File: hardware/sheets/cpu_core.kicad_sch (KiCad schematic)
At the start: 25 parts, among them U1 V20, U10 74HC32, U11 74HC08, U12 74HC157, U13 74HC04, U14 TCM809, U15 74HC08, U2 74HC573, U3 74HC573, U4 74HC573, U5 74HC245, U6 74HCT138, U7 74HC00, U8 74HC74, U9 74HC4017

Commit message: Standardize 5V glue on 74HCT; fix bus-latch family; div-3 -> 74HCT163
All 5V 74-series logic moved from mixed HC/HCT to 74HCT (TTL thresholds reliably
read 3.3V level-shifter outputs). Fixes the address latches / data transceiver
that were wrongly 74HC instead of the design's 74HCT. The div-by-3 moves from
74HC4017 (no HCT variant) to a 74HCT163 preset-to-3 with a spare 74HCT04 gate
for the TC->~PE reload. Per-card level shifters use a dedicated 74LVC245A symbol.
Pinouts unchanged; netlist intact; zero structural ERC errors.

Co-Authored-By: Claude Opus 4.8 (1M context) <noreply@anthropic.com>
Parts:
- removed U10: 74HC32, symbol mini-xt:74HC32
- removed U11, U15: 74HC08, symbol mini-xt:74HC08
- removed U12: 74HC157, symbol mini-xt:74HC157
- removed U13: 74HC04, symbol mini-xt:74HC04
- removed U2, U3, U4: 74HC573, symbol mini-xt:74HC573
- removed U5: 74HC245, symbol mini-xt:74HC245
- removed U7: 74HC00, symbol mini-xt:74HC00
- removed U8: 74HC74, symbol mini-xt:74HC74
- removed U9: 74HC4017, symbol mini-xt:74HC4017
- added U10: 74HCT32, symbol mini-xt:74HCT32
- added U11, U15: 74HCT08, symbol mini-xt:74HCT08
- added U12: 74HCT157, symbol mini-xt:74HCT157
- added U13: 74HCT04, symbol mini-xt:74HCT04
- added U2, U3, U4: 74HCT573, symbol mini-xt:74HCT573
- added U5: 74HCT245, symbol mini-xt:74HCT245
- added U7: 74HCT00, symbol mini-xt:74HCT00
- added U8: 74HCT74, symbol mini-xt:74HCT74
- added U9: 74HCT163, symbol mini-xt:74HCT163
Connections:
- net +5V: now also U10.14 (VCC), U11.14 (VCC), U12.16 (VCC), U13.14 (VCC), U15.14 (VCC), U2.20 (VCC), U3.20 (VCC), U4.20 (VCC), U5.20 (VCC), U7.14 (VCC), U8.1 (~{R}), U8.14 (VCC), U8.4 (~{S}), U9.1 (~{MR}), U9.10 (CET), U9.16 (VCC), U9.3 (D0), U9.5 (D2), U9.6 (D3), U9.7 (CEP)
- net A0: now also U2.19 (Q0)
- net A1: now also U2.18 (Q1)
- net A10: now also U3.17 (Q2)
- net A11: now also U3.16 (Q3)
- net A12: now also U3.15 (Q4)
- net A13: now also U3.14 (Q5)
- net A14: now also U3.13 (Q6)
- net A15: now also U3.12 (Q7)
- net A16: now also U4.19 (Q0)
- net A17: now also U4.18 (Q1)
- net A18: now also U4.17 (Q2)
- net A19: now also U4.16 (Q3), U7.1 (P1)
- net A2: now also U2.17 (Q2)
- net A3: now also U2.16 (Q3)
- net A4: now also U2.15 (Q4)
- net A5: now also U2.14 (Q5)
- net A6: now also U2.13 (Q6)
- net A7: now also U2.12 (Q7)
- net A8: now also U3.19 (Q0)
- net A9: now also U3.18 (Q1)
- net AD0: now also U2.2 (D0), U5.2 (A0)
- net AD1: now also U2.3 (D1), U5.3 (A1)
- net AD2: now also U2.4 (D2), U5.4 (A2)
- net AD3: now also U2.5 (D3), U5.5 (A3)
- net AD4: now also U2.6 (D4), U5.6 (A4)
- net AD5: now also U2.7 (D5), U5.7 (A5)
- net AD6: now also U2.8 (D6), U5.8 (A6)
- net AD7: now also U2.9 (D7), U5.9 (A7)
- net BALE_L: now also U2.11 (Load), U3.11 (Load), U4.11 (Load)
- net CLK: now also U13.4 (P4)
- net CLK4: now also U12.3 (I1a), U9.14 (Q0)
- net CLK7: now also U12.2 (I0a), U13.3 (P3), U8.5 (Q)
- net CLK_MUX: now also U12.4 (Za), U13.1 (P1)
- net CLK_QN: now also U8.2 (D), U8.6 (~{Q})
- net CPUCLK: now also U13.2 (P2)
- net D0: now also U5.18 (B0)
- net D1: now also U5.17 (B1)
- net D2: now also U5.16 (B2)
- net D3: now also U5.15 (B3)
- net D4: now also U5.14 (B4)
- net D5: now also U5.13 (B5)
- net D6: now also U5.12 (B6)
- net D7: now also U5.11 (B7)
- net GND: now also U10.7 (GND), U11.7 (GND), U12.15 (E), U12.8 (GND), U13.7 (GND), U15.7 (GND), U2.1 (OE), U2.10 (GND), U3.1 (OE), U3.10 (GND), U4.1 (OE), U4.10 (GND), U5.10 (GND), U5.19 (CE), U7.7 (GND), U8.7 (GND), U9.4 (D1), U9.8 (GND)
- net MA10: now also U3.4 (D2)
- net MA11: now also U3.5 (D3)
- net MA12: now also U3.6 (D4)
- net MA13: now also U3.7 (D5)
- net MA14: now also U3.8 (D6)
- net MA15: now also U3.9 (D7)
- net MA16: now also U4.2 (D0)
- net MA17: now also U4.3 (D1)
- net MA18: now also U4.4 (D2)
- net MA19: now also U4.5 (D3)
- net MA8: now also U3.2 (D0)
- net MA9: now also U3.3 (D1)
- net OSC: now also U8.3 (C), U9.2 (CP)
- net RAM2_CE: now also U7.3 (P3)
- net SPEED_SEL: now also U12.1 (S)
- net Y5_INT: now also U7.2 (P2)
- net ~{IOR}: now also U10.13 (P13)
- net ~{IOW}: now also U11.13 (P13)
- net ~{MEMR}: now also U10.1 (P1)
- net ~{MEMW}: now also U11.1 (P1)
- net ~{RD}: now also U5.1 (A->B)
- new net DIV3_LD: U13.6 (P6), U9.9 (~{PE})
- new net DIV3_TC: U13.5 (P5), U9.15 (TC)

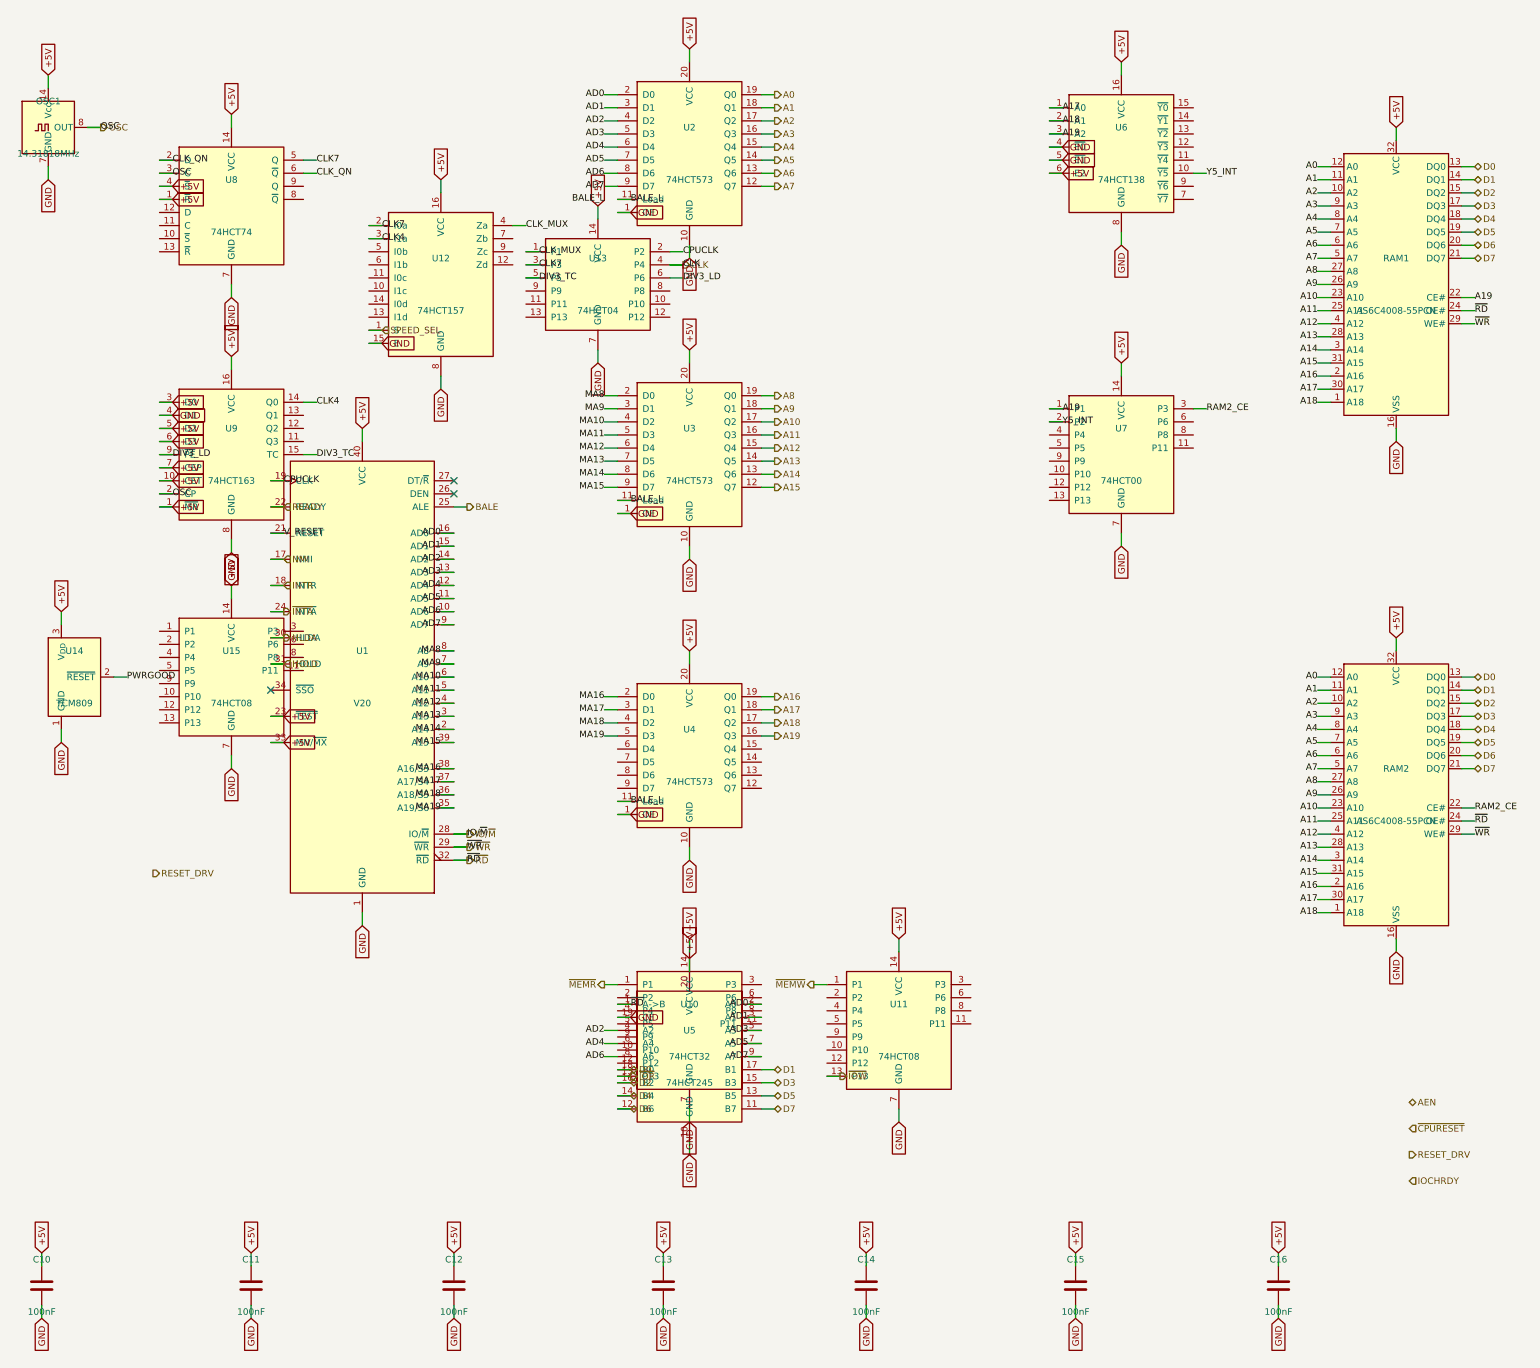
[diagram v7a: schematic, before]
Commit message: Fix all critical+high design-review findings (C1-C5, H1-H8)
Full review in hardware/notes/design-review-2026-07-03.md (with per-item
fix logs). Highlights:
- SRAM strobed by gated MEMR/MEMW (was raw ~RD/~WR: I/O cycles corrupted
  SRAM and the boot shadow-load could never write it)
- Reset chain implemented: NAND combine of ~PWRGOOD + ~CPURESET drives
  V20 RESET and an always-driven RESET_DRV (dropped from the Bus MCU)
- Contention-free bus handoff: '573 OE=HLDA vs counter '244 stage
  ~OE=~HLDA; strobe gates wired + tri-stated ('125, ~OE=HLDA); Bus MCU
  address group fixed to sense; AEN/TC fixed drive; BALE input-only
- '573 LE driven by BALE (was a dangling BALE_L label)
- Data '245 DIR=DT/~R, ~OE=DEN so INTA vectors reach the CPU
- Idle pulls: strobes/DEN high, AEN/IRQ2-9/DRQ low, IOCHRDY/IOCHCK/
  DACK2-3 high
- CH224K CFG1 left open (grounding it selects 9-20V, not 5V)
- XT-IDE INTRQ pull-down (pull-up parked IRQ5 asserted)
- LPT status bit7 = ~Busy via spare inverter (SPP semantics)
- Audio summer TL072 -> MCP6002 (RRIO; TL072 out of spec at +5V single
  supply)
- card_isatest: DUT P-FET gate to V5RAW + NPN driver (default off, can
  fully turn off); /3 divider TC->~PE reload actually wired

Overturned picks corrected in notes/questions-*.md. All sheets + cards
rebuilt; structural ERC = 0; fixes netlist-verified.

Co-Authored-By: Claude Fable 5 <noreply@anthropic.com>
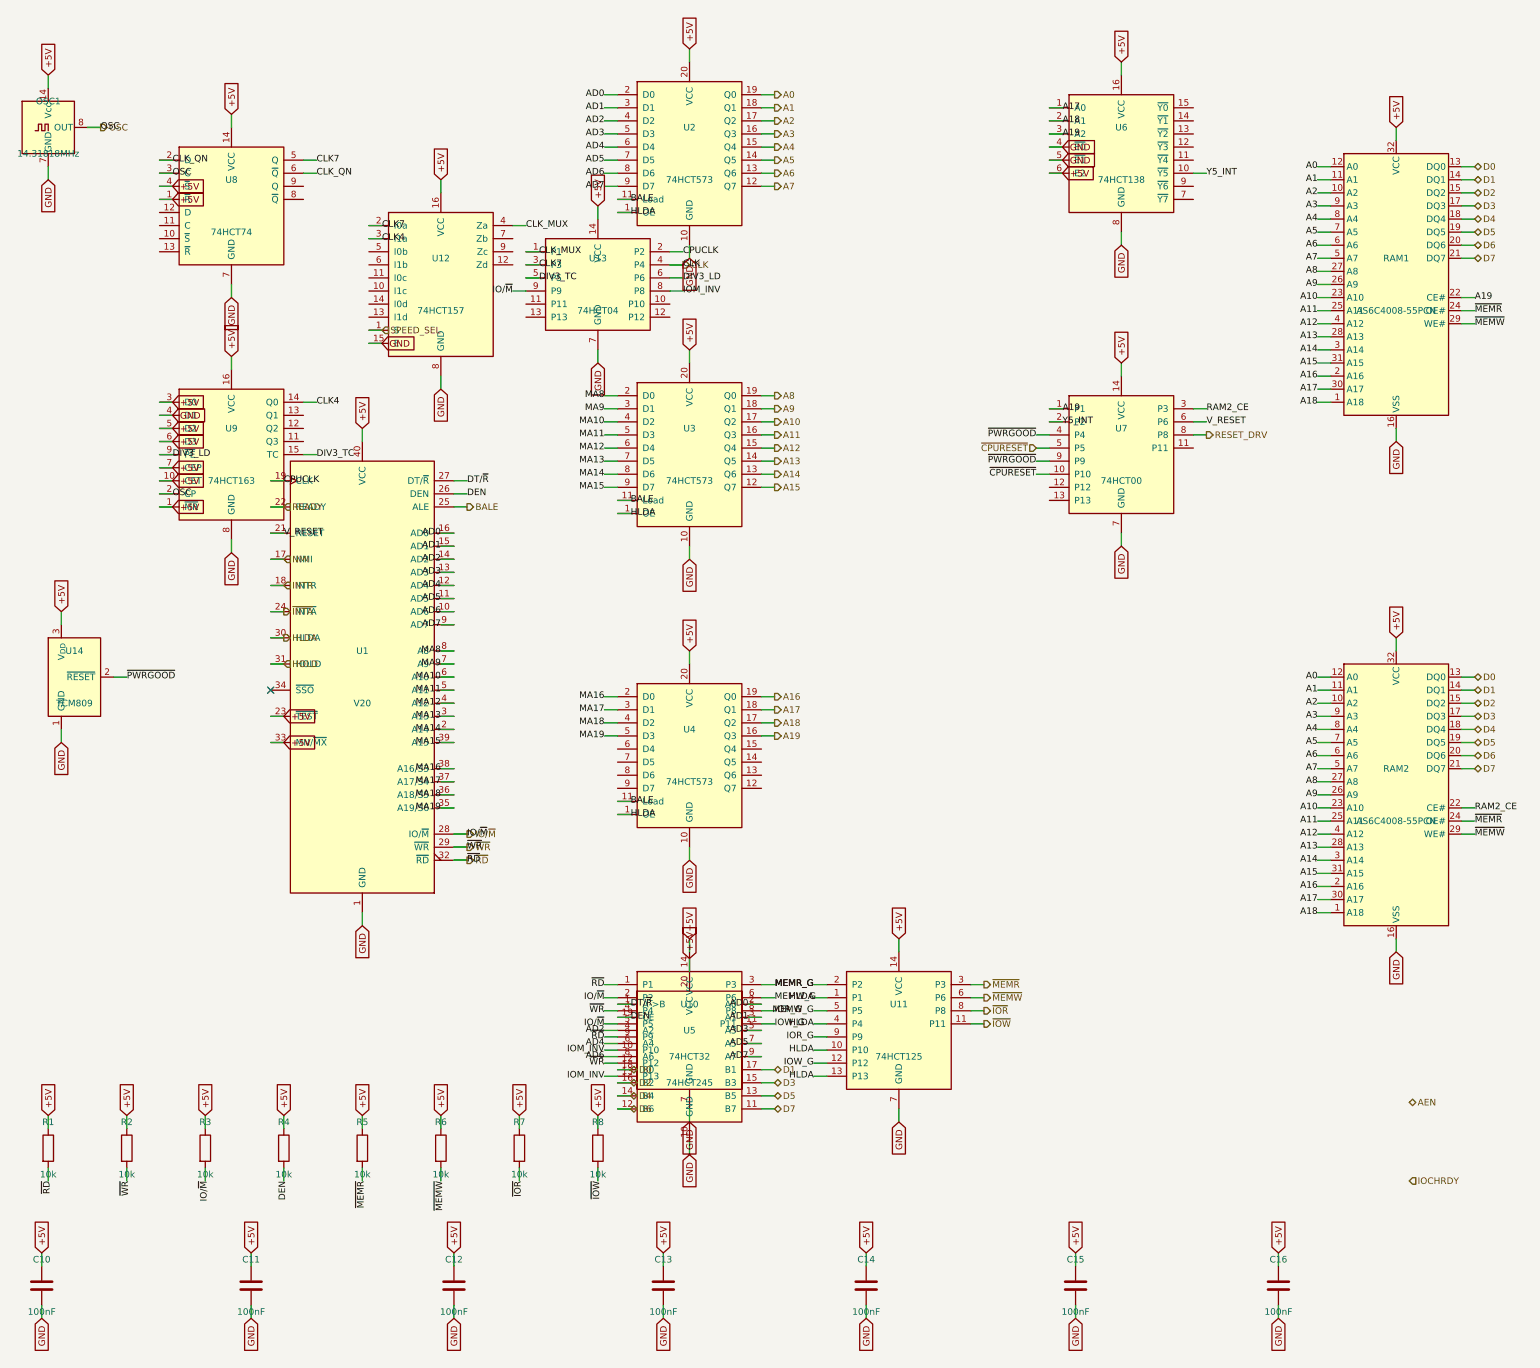
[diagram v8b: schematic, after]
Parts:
- removed U11, U15: 74HCT08, symbol mini-xt:74HCT08
- added R1, R2, R3, R4, R5, R6, R7, R8: 10k, symbol Device:R
- added U11: 74HCT125, symbol mini-xt:74HCT125
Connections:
- net BALE_L is gone; now on net BALE: U2.11 (Load), U3.11 (Load), U4.11 (Load)
- net PWRGOOD is gone; now on net ~{PWRGOOD}: U14.2 (~{RESET})
- net +5V: now also R1.1, R2.1, R3.1, R4.1, R5.1, R6.1, R7.1, R8.1, U11.14 (VCC)
- net GND: now also U11.7 (GND); no longer U2.1 (OE), U3.1 (OE), U4.1 (OE), U5.19 (CE)
- net HLDA: now also U2.1 (OE), U3.1 (OE), U4.1 (OE), U11.1 (P1), U11.10 (P10), U11.13 (P13), U11.4 (P4)
- net IO/~{M}: now also U10.2 (P2), U10.5 (P5), U13.9 (P9), R3.2
- net RESET_DRV: now also U7.8 (P8)
- net V_RESET: now also U7.6 (P6)
- net ~{CPURESET}: now also U7.10 (P10), U7.5 (P5)
- net ~{IOR}: now also R7.2, U11.8 (P8); no longer U10.13 (P13)
- net ~{IOW}: now also R8.2, U11.11 (P11)
- net ~{MEMR}: now also RAM1.24 (OE#), RAM2.24 (OE#), R5.2, U11.3 (P3); no longer U10.1 (P1)
- net ~{MEMW}: now also RAM1.29 (WE#), RAM2.29 (WE#), R6.2, U11.6 (P6)
- net ~{RD}: now also U10.1 (P1), U10.9 (P9), R1.2; no longer RAM1.24 (OE#), RAM2.24 (OE#), U5.1 (A->B)
- net ~{WR}: now also U10.12 (P12), U10.4 (P4), R2.2; no longer RAM1.29 (WE#), RAM2.29 (WE#)
- net IOM_INV: now reaches U10.10 (P10)
- net IOM_INV: now also U10.13 (P13), U13.8 (P8)
- net IOW_G: now reaches U10.11 (P11)
- net IOW_G: now also U11.12 (P12)
- net MEMR_G: now reaches U10.3 (P3)
- net MEMR_G: now also U11.2 (P2)
- net MEMW_G: now reaches U10.6 (P6)
- net MEMW_G: now also U11.5 (P5)
- net IOR_G: now reaches U10.8 (P8)
- net IOR_G: now also U11.9 (P9)
- net DEN: now reaches U1.26 (DEN)
- net DEN: now also U5.19 (CE), R4.2
- net DT/~{R}: now reaches U1.27 (DT/~{R})
- net DT/~{R}: now also U5.1 (A->B)
- net ~{PWRGOOD}: now reaches U7.4 (P4)
- net ~{PWRGOOD}: now also U7.9 (P9)
- no-connect marks 3 -> 1
